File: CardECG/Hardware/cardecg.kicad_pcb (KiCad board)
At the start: 2 copper layers, 57 parts, among them CN1 2TAP, P1 PROG, P2 BATTERY, P3 FORCE ON, Q1 BSS84P, Q2 NTR1P02T1, Q3 BSS84P, Q4 NTR1P02T1, Q5 NMOS_GSD, Q6 NMOS_GSD, Q7 NTR1P02T1, U1 LMV341, U2 TPS717, U3 ADuC7061, U4 SSD1306, U5 creditcard, U6 DNP, U7 DNP

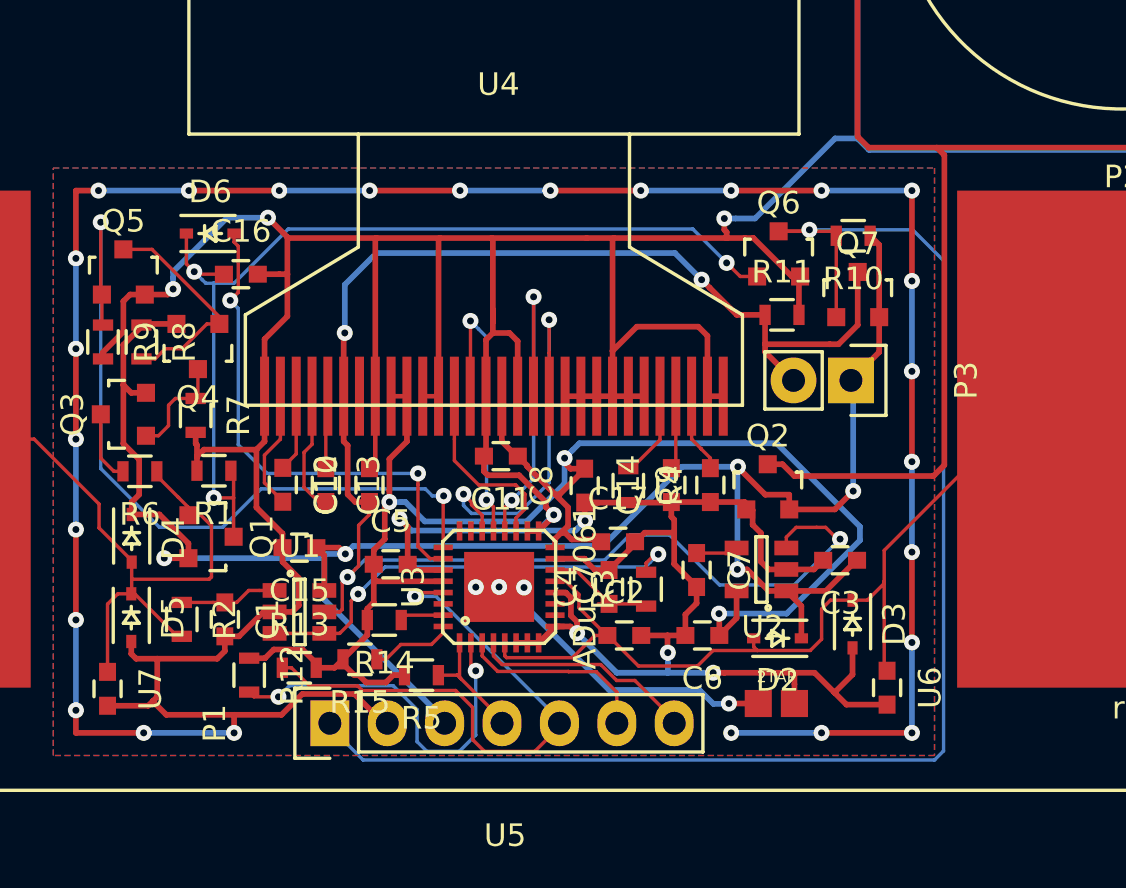
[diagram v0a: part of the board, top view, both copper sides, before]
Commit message: Fix CardECG power feedback from display.
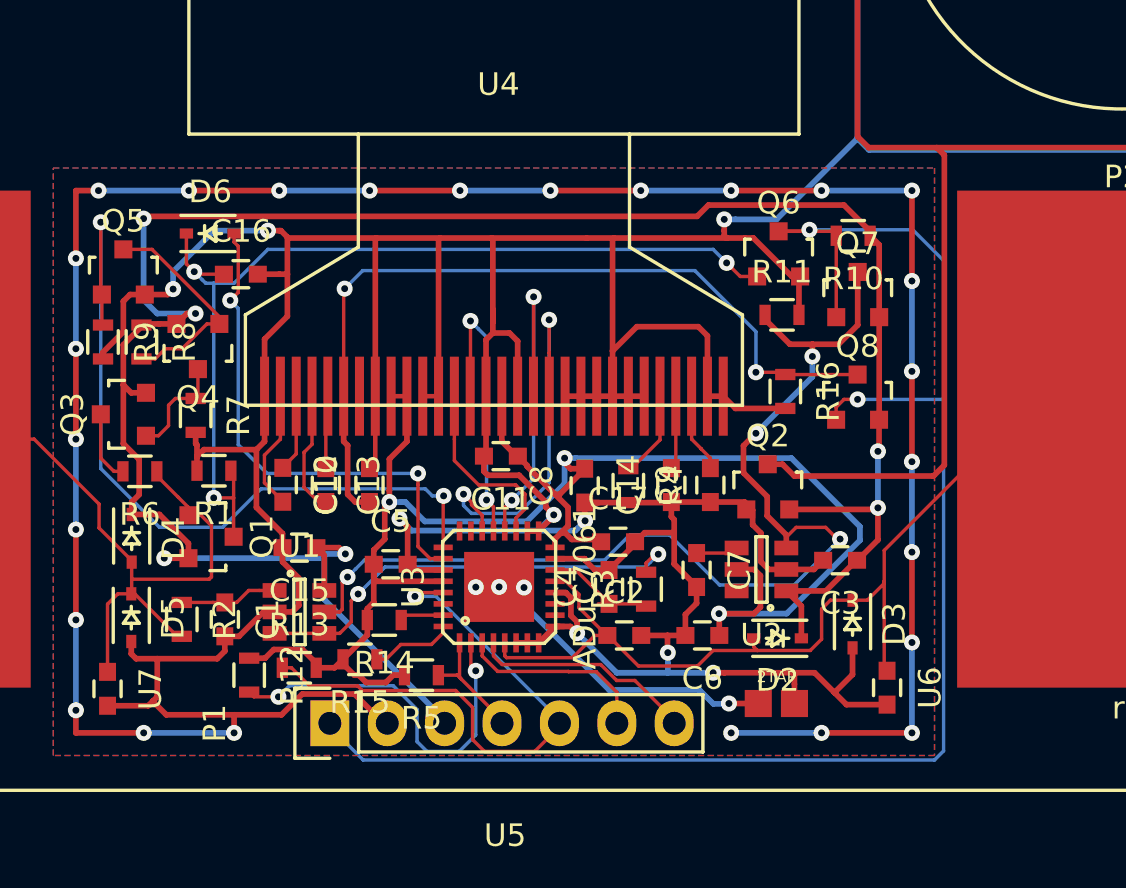
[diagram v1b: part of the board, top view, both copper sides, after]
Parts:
- removed P3: FORCE ON, Pin_Headers:Pin_Header_Straight_1x02
- added Q8: NTR1P02T1, TO_SOT_Packages_SMD:SOT-23, F.Cu at (84.6, 59.6)
- added R16: 100k, Resistors_SMD:R_0603, F.Cu at (81.4, 59.4)
- Q1, Q3: value BSS84P -> NTR1P02T1; footprint Housings_SOT-23_SOT-143_TSOT-6:SOT-23 -> TO_SOT_Packages_SMD:SOT-23
- Q2, Q4, Q5, Q6, Q7: footprint Housings_SOT-23_SOT-143_TSOT-6:SOT-23 -> TO_SOT_Packages_SMD:SOT-23
- U1: footprint Housings_SOT-23_SOT-143_TSOT-6:SOT-23-6 -> TO_SOT_Packages_SMD:SOT-23-6
- U2: footprint Housings_SOT-23_SOT-143_TSOT-6:SOT-23-5 -> TO_SOT_Packages_SMD:SOT-23-6
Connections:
- C10 pad 1: VCC -> OLED_PWR
- U4 pad 6: VCC -> OLED_PWR
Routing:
- net OLED_PWR: track 0.00 -> 36.3 mm, vias 0 -> 2
- net VCC: track 74.7 -> 48.5 mm
- net +BATT: track 89.1 -> 103.5 mm, vias 5 -> 6
- net ~FORCE_ON: track 64.1 -> 69.5 mm, vias 1 -> 2
- net GND: track 366.5 -> 369.0 mm
- net VDD: track 74.9 -> 76.6 mm
- net Net-(C16-Pad1): track 43.8 -> 43.1 mm
